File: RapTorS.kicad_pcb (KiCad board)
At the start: 2 copper layers, 45 x 19 mm, 22 parts, among them J1 Molex 48037-2200, J2 TestPoint, J3 TestPoint, J4 TestPoint, J5 TestPoint, J6 TestPoint, U1 PIC16LF1454-I_ML, U2 TLV71333PDBV, U3 E07-M1101S

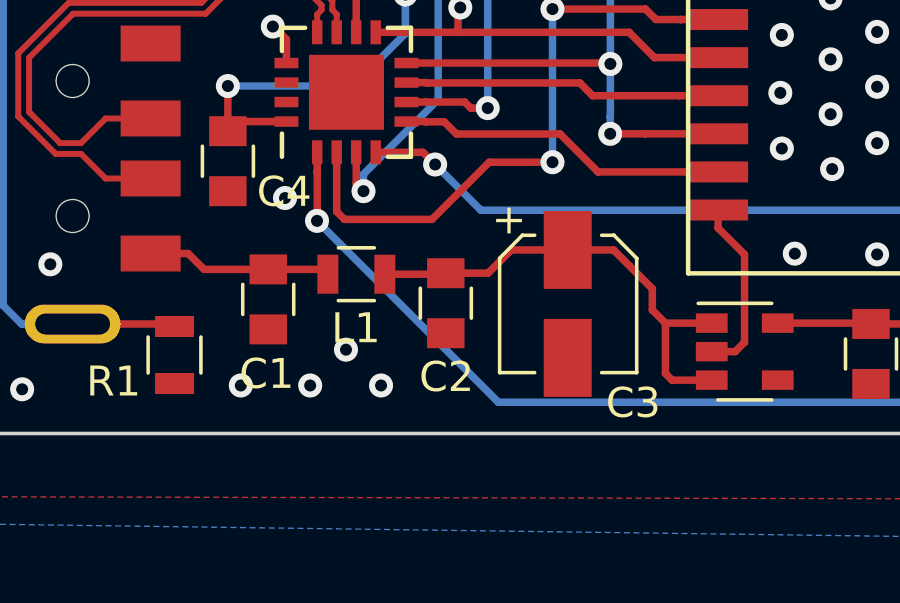
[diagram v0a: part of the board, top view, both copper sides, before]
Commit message: update C3 on layout, generate gerber
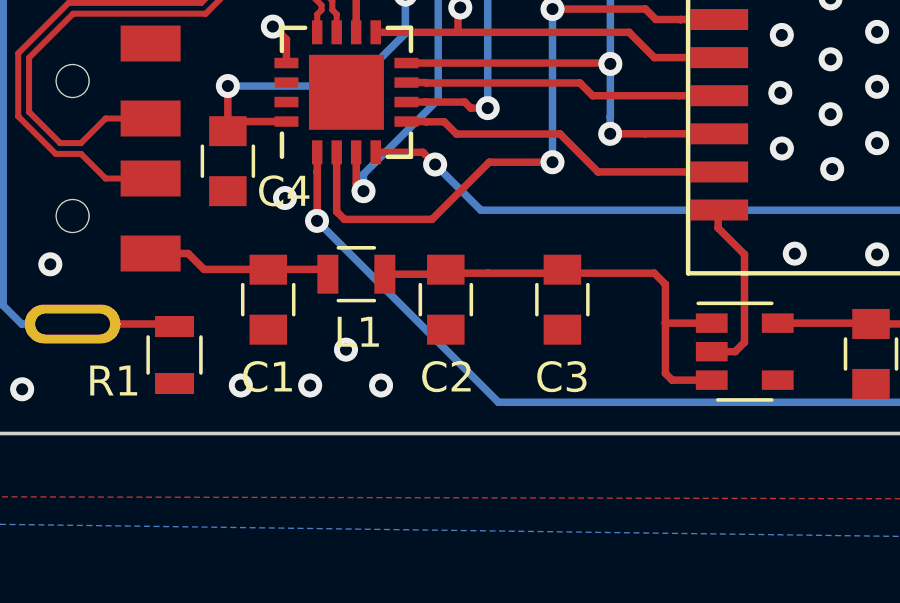
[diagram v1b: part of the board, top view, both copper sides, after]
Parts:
- C3: footprint Capacitors_SMD:CP_Elec_4x4.5 -> Capacitors_SMD:C_0805
- moved C3 0.23 mm to (157.8, 105.7)
- moved C2 0.12 mm to (153.9, 105.7)
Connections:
- U2 pad 4: (no net) -> Net-(U2-Pad4)
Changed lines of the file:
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@@
-(kicad_pcb (version 20171130) (host pcbnew "(6.0.0-rc1-dev-437-ga2d36a674-dirty)")
+(kicad_pcb (version 20171130) (host pcbnew "(6.0.0-rc1-dev-438-g6845ac2cc-dirty)")
   (general
     (thickness 1.6)
     (drawings 19)
-    (tracks 228)
+    (tracks 226)
     (zones 0)
     (modules 22)
-    (nets 20)
+    (nets 21)
   )
   (page A4)
@@
   (net 18 CSN)
   (net 19 "Net-(ANT1-Pad1)")
+  (net 20 "Net-(U2-Pad4)")
   (net_class Default "Ceci est la Netclass par défaut."
     (clearance 0.16)
@@
     (add_net "Net-(D2-Pad2)")
     (add_net "Net-(J1-Pad5)")
+    (add_net "Net-(U2-Pad4)")
     (add_net ~MCLR)
+  )
+  (module Capacitors_SMD:C_0805 (layer F.Cu)
+    (at 157.8356 105.7 270)
+    (descr "Capacitor SMD 0805, reflow soldering, AVX (see smccp.pdf)")
+    (tags "capacitor 0805")
+    (attr smd)
+    (fp_text reference C3 (at 2.6 0) (layer F.SilkS)
+      (effects (font (size 1 1) (thickness 0.15)))
+    )
+    (fp_text value 4.7uF (at 0 1.75 270) (layer F.Fab)
+      (effects (font (size 1 1) (thickness 0.15)))
+    )
+    (fp_text user %R (at 0 -1.5 270) (layer F.Fab)
+      (effects (font (size 1 1) (thickness 0.15)))
+    )
+    (fp_line (start -1 0.62) (end -1 -0.62) (layer F.Fab) (width 0.1))
+    (fp_line (start 1 0.62) (end -1 0.62) (layer F.Fab) (width 0.1))
+    (fp_line (start 1 -0.62) (end 1 0.62) (layer F.Fab) (width 0.1))
+    (fp_line (start -1 -0.62) (end 1 -0.62) (layer F.Fab) (width 0.1))
+    (fp_line (start 0.5 -0.85) (end -0.5 -0.85) (layer F.SilkS) (width 0.12))
+    (fp_line (start -0.5 0.85) (end 0.5 0.85) (layer F.SilkS) (width 0.12))
+    (fp_line (start -1.75 -0.88) (end 1.75 -0.88) (layer F.CrtYd) (width 0.05))
+    (fp_line (start -1.75 -0.88) (end -1.75 0.87) (layer F.CrtYd) (width 0.05))
+    (fp_line (start 1.75 0.87) (end 1.75 -0.88) (layer F.CrtYd) (width 0.05))
+    (fp_line (start 1.75 0.87) (end -1.75 0.87) (layer F.CrtYd) (width 0.05))
+    (pad 1 smd rect (at -1 0 270) (size 1 1.25) (layers F.Cu F.Paste F.Mask)
+      (net 2 +5V))
+    (pad 2 smd rect (at 1 0 270) (size 1 1.25) (layers F.Cu F.Paste F.Mask)
+      (net 3 GND))
+    (model ${KISYS3DMOD}/Capacitor_SMD.3dshapes/C_0805_2012Metric.wrl
+      (at (xyz 0 0 0))
+      (scale (xyz 1 1 1))
+      (rotate (xyz 0 0 0))
+    )
   )
   (module Logo:Logo (layer B.Cu)
@@
       (net 17 ~MCLR))
   )
-  (module Capacitors_SMD:CP_Elec_4x4.5 (layer F.Cu)
-    (at 158.0134 105.8418 270)
-    (descr "SMT capacitor, aluminium electrolytic, 4x4.5")
-    (attr smd)
-    (fp_text reference C3 (at 3.302 -2.1844 180) (layer F.SilkS)
-      (effects (font (size 1 1) (thickness 0.15)))
-    )
-    (fp_text value 4.7uF (at 0 -3.45 90) (layer F.Fab) hide
-      (effects (font (size 1 1) (thickness 0.15)))
-    )
-    (fp_circle (center 0 0) (end 0.1 2.1) (layer F.Fab) (width 0.1))
-    (fp_text user + (at -1.24 -0.08 270) (layer F.Fab)
-      (effects (font (size 1 1) (thickness 0.15)))
-    )
-    (fp_text user + (at -2.78 1.99 90) (layer F.SilkS)
-      (effects (font (size 1 1) (thickness 0.15)))
-    )
-    (fp_text user %R (at 0.2032 1.5748 90) (layer F.Fab)
-      (effects (font (size 1 1) (thickness 0.15)))
-    )
-    (fp_line (start 2.13 2.12) (end 2.13 -2.15) (layer F.Fab) (width 0.1))
-    (fp_line (start -1.46 2.12) (end 2.13 2.12) (layer F.Fab) (width 0.1))
-    (fp_line (start -2.13 1.45) (end -1.46 2.12) (layer F.Fab) (width 0.1))
-    (fp_line (start -2.13 -1.47) (end -2.13 1.45) (layer F.Fab) (width 0.1))
-    (fp_line (start -1.46 -2.15) (end -2.13 -1.47) (layer F.Fab) (width 0.1))
-    (fp_line (start 2.13 -2.15) (end -1.46 -2.15) (layer F.Fab) (width 0.1))
-    (fp_line (start 2.29 -2.3) (end 2.29 -1.13) (layer F.SilkS) (width 0.12))
-    (fp_line (start 2.29 2.27) (end 2.29 1.1) (layer F.SilkS) (width 0.12))
-    (fp_line (start -2.29 1.51) (end -2.29 1.1) (layer F.SilkS) (width 0.12))
-    (fp_line (start -2.29 -1.54) (end -2.29 -1.13) (layer F.SilkS) (width 0.12))
-    (fp_line (start -1.52 -2.3) (end 2.29 -2.3) (layer F.SilkS) (width 0.12))
-    (fp_line (start -1.52 -2.3) (end -2.29 -1.54) (layer F.SilkS) (width 0.12))
-    (fp_line (start -1.52 2.27) (end 2.29 2.27) (layer F.SilkS) (width 0.12))
-    (fp_line (start -1.52 2.27) (end -2.29 1.51) (layer F.SilkS) (width 0.12))
-    (fp_line (start -3.35 -2.4) (end 3.35 -2.4) (layer F.CrtYd) (width 0.05))
-    (fp_line (start -3.35 -2.4) (end -3.35 2.37) (layer F.CrtYd) (width 0.05))
-    (fp_line (start 3.35 2.37) (end 3.35 -2.4) (layer F.CrtYd) (width 0.05))
-    (fp_line (start 3.35 2.37) (end -3.35 2.37) (layer F.CrtYd) (width 0.05))
-    (pad 1 smd rect (at -1.8 0 90) (size 2.6 1.6) (layers F.Cu F.Paste F.Mask)
-      (net 2 +5V))
-    (pad 2 smd rect (at 1.8 0 90) (size 2.6 1.6) (layers F.Cu F.Paste F.Mask)
-      (net 3 GND))
-    (model ${KISYS3DMOD}/Capacitor_SMD.3dshapes/CP_Elec_4x4.5.wrl
-      (at (xyz 0 0 0))
-      (scale (xyz 1 1 1))
-      (rotate (xyz 0 0 0))
-    )
-  )
   (module Capacitors_SMD:C_0805 (layer F.Cu)
     (at 168.1226 107.5088 270)
@@
   )
   (module Capacitors_SMD:C_0805 (layer F.Cu)
-    (at 153.9494 105.8164 270)
+    (at 153.9494 105.7 270)
     (descr "Capacitor SMD 0805, reflow soldering, AVX (see smccp.pdf)")
     (tags "capacitor 0805")
     (attr smd)
-    (fp_text reference C2 (at 2.4638 -0.0254) (layer F.SilkS)
+    (fp_text reference C2 (at 2.6 -0.0508) (layer F.SilkS)
       (effects (font (size 1 1) (thickness 0.15)))
     )
@@
   )
   (module Capacitors_SMD:C_0805 (layer F.Cu)
-    (at 148.0312 105.6894 270)
+    (at 148.0312 105.7 270)
     (descr "Capacitor SMD 0805, reflow soldering, AVX (see smccp.pdf)")
     (tags "capacitor 0805")
     (attr smd)
-    (fp_text reference C1 (at 2.4892 0.0508) (layer F.SilkS)
+    (fp_text reference C1 (at 2.6 0) (layer F.SilkS)
       (effects (font (size 1 1) (thickness 0.15)))
     )
@@
     (tags "resistor 0805")
     (attr smd)
-    (fp_text reference L1 (at -0.0152 1.8034) (layer F.SilkS)
+    (fp_text reference L1 (at 0.061 1.9558) (layer F.SilkS)
       (effects (font (size 1 1) (thickness 0.15)))
     )
@@
     (pad 3 smd rect (at -1.1 0.95) (size 1.06 0.65) (layers F.Cu F.Paste F.Mask)
       (net 2 +5V))
-    (pad 4 smd rect (at 1.1 0.95) (size 1.06 0.65) (layers F.Cu F.Paste F.Mask))
+    (pad 4 smd rect (at 1.1 0.95) (size 1.06 0.65) (layers F.Cu F.Paste F.Mask)
+      (net 20 "Net-(U2-Pad4)"))
     (pad 5 smd rect (at 1.1 -0.95) (size 1.06 0.65) (layers F.Cu F.Paste F.Mask)
       (net 1 +3V3))
@@
   (segment (start 149.51054 93.93614) (end 149.51054 94.2086) (width 0.25) (layer F.Cu) (net 1))
   (segment (start 149.3012 93.7268) (end 149.51054 93.93614) (width 0.25) (layer F.Cu) (net 1))
-  (segment (start 158.0134 104.0418) (end 159.5408 104.0418) (width 0.25) (layer F.Cu) (net 2))
-  (segment (start 159.5408 104.0418) (end 160.8328 105.3338) (width 0.25) (layer F.Cu) (net 2))
-  (segment (start 160.8328 105.3338) (end 160.8328 106.045) (width 0.25) (layer F.Cu) (net 2))
   (segment (start 161.2696 106.4818) (end 162.814 106.4818) (width 0.25) (layer F.Cu) (net 2))
-  (segment (start 160.8328 106.045) (end 161.2696 106.4818) (width 0.25) (layer F.Cu) (net 2))
   (segment (start 161.2696 106.4818) (end 161.2696 108.1582) (width 0.25) (layer F.Cu) (net 2))
   (segment (start 161.4932 108.3818) (end 162.814 108.3818) (width 0.25) (layer F.Cu) (net 2))
@@
   (segment (start 153.9146 104.8512) (end 153.9494 104.8164) (width 0.25) (layer F.Cu) (net 2))
   (segment (start 151.9174 104.8512) (end 153.9146 104.8512) (width 0.25) (layer F.Cu) (net 2))
-  (segment (start 156.1304 104.0418) (end 158.0134 104.0418) (width 0.25) (layer F.Cu) (net 2))
-  (segment (start 155.3558 104.8164) (end 156.1304 104.0418) (width 0.25) (layer F.Cu) (net 2))
   (segment (start 153.9494 104.8164) (end 155.3558 104.8164) (width 0.25) (layer F.Cu) (net 2))
+  (segment (start 155.3558 104.8164) (end 157.8356 104.8164) (width 0.25) (layer F.Cu) (net 2))
+  (segment (start 157.8356 104.8164) (end 160.8996 104.8164) (width 0.25) (layer F.Cu) (net 2))
+  (segment (start 161.2696 105.1864) (end 161.2696 106.4818) (width 0.25) (layer F.Cu) (net 2))
+  (segment (start 160.8996 104.8164) (end 161.2696 105.1864) (width 0.25) (layer F.Cu) (net 2))
   (via (at 140.7668 104.521) (size 0.8) (drill 0.4) (layers F.Cu B.Cu) (net 3))
   (segment (start 163.594 107.4318) (end 163.9062 107.1196) (width 0.25) (layer F.Cu) (net 3))
